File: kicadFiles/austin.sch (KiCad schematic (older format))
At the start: 465 parts, among them J1 TYPE-C-31-M12_13, J2 Conn_01x04_Male, J5 Conn_01x06_Male, Q1 AO4406AL, SW1 MXSwitch, SW10 MXSwitch, SW100 MXSwitch, SW101 MXSwitch, SW102 MXSwitch, SW103 MXSwitch, SW104 MXSwitch, SW105 MXSwitch, SW106 MXSwitch, SW107 MXSwitch, SW108 MXSwitch, SW109 MXSwitch, SW11 MXSwitch, SW110 MXSwitch, SW111 MXSwitch, SW112 MXSwitch, SW12 MXSwitch, SW13 MXSwitch, SW14 MXSwitch, SW15 MXSwitch, SW16 MXSwitch, SW17 MXSwitch, SW18 MXSwitch, SW19 MXSwitch, SW2 MXSwitch, SW20 MXSwitch, SW21 MXSwitch, SW22 MXSwitch, SW23 MXSwitch, SW24 MXSwitch, SW25 MXSwitch, SW26 MXSwitch, SW27 MXSwitch, SW28 MXSwitch, SW29 MXSwitch, SW3 MXSwitch, SW30 MXSwitch, SW31 MXSwitch, SW32 MXSwitch, SW33 MXSwitch, SW34 MXSwitch, SW35 MXSwitch, SW36 MXSwitch, SW37 MXSwitch, SW38 MXSwitch, SW39 MXSwitch, SW4 MXSwitch, SW40 MXSwitch, SW41 MXSwitch, SW42 MXSwitch, SW43 MXSwitch, SW44 MXSwitch, SW45 MXSwitch, SW46 MXSwitch, SW47 MXSwitch, SW48 MXSwitch, SW49 MXSwitch, SW5 MXSwitch, SW50 MXSwitch, SW51 MXSwitch, SW52 MXSwitch, SW53 MXSwitch, SW54 MXSwitch, SW55 MXSwitch, SW56 MXSwitch, SW57 MXSwitch, SW58 MXSwitch, SW59 MXSwitch, SW6 MXSwitch, SW60 MXSwitch, SW61 MXSwitch, SW62 MXSwitch, SW63 MXSwitch, SW64 MXSwitch, SW65 MXSwitch, SW66 MXSwitch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

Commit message: [Pre-release] V1.0 pre-release
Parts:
- added LEDCAPS1, LEDNUM1, LEDSCRL1: LED, acheronComponents:thtLED, symbol acheronSymbols:LED
- added RI1, RI2, RI3: 360, acheronComponents:R_1026, symbol Device:R_Small
- CB4: renamed from CVB4; value 1u -> 100n
- CB5: renamed from CVB5; value 4.7u -> 10u
- SW111: footprint acheronKeyboardSwitches:MX700 -> acheronKeyboardSwitches:MX700R
- renumbered CVB1 to CB1, CVB2 to CB2, CVB3 to CB3, CSin1 to CRI1, CSout1 to CRO1, D63 to D100, D65 to D101, D66 to D102, D71 to D103, D79 to D104, D85 to D105, D91 to D106, D97 to D107, D103 to D108, D67 to D13, D72 to D14, D75 to D15, D80 to D16, D86 to D17, D92 to D18, D98 to D19, D13 to D20, D14 to D21, D15 to D22, D16 to D23, D17 to D24, D18 to D25, D19 to D26, D20 to D27, D21 to D28, D22 to D29, D23 to D30, D24 to D31, D68 to D32, D73 to D33, D76 to D35, D81 to D36, D87 to D37, D93 to D38, D99 to D39, D25 to D40, D26 to D41, D27 to D42, D28 to D43, D29 to D44, D30 to D45, D31 to D46, D32 to D47, D33 to D48, D34 to D49, D35 to D50, D36 to D51, D69 to D52, D74 to D53, D77 to D54, D82 to D55, D88 to D56, D94 to D57, D100 to D59, D37 to D61, D38 to D62, D39 to D63, D40 to D64, D41 to D65, D42 to D66, D43 to D67, D44 to D68, D45 to D69, D46 to D70, D47 to D71, D104 to D72, D48 to D73, D78 to D74, D83 to D75, D89 to D76, D95 to D77, D101 to D78, D49 to D79, D51 to D80, D53 to D81, D55 to D82, D56 to D83, D57 to D84, D59 to D85, D60 to D86, D61 to D87, D62 to D88, D64 to D89, D105 to D90, D70 to D91, D84 to D92, D90 to D93, D96 to D94, D102 to D95, D50 to D96, D52 to D97, D54 to D98, D58 to D99, RPGate1 to RGP1, RSGate1 to RGS1, R72 to RL72
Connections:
- net labels added: CAPSLCK, NUMLCK, SCRLLCK
- wire segments 943 -> 952
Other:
- note added: "CBs for "Capacitors - Bypass""
- note added: "DF for "Diode - Fuse""
- note added: "DS33 for "Schottky Diode - 3.3V""
- note added: "RGP for "Gate Parallel"\nRGS for "Gate Series""

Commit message: [Update] Version 1.1
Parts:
- removed U2: MCP1700-3302E_SOT23, Package_TO_SOT_SMD:SOT-23, symbol Regulator_Linear:MCP1700-3302E_SOT23
- added U2: TLV1117-33, Package_TO_SOT_SMD:SOT-223-3_TabPin2, symbol Regulator_Linear:TLV1117-33
- U3: footprint Package_TO_SOT_SMD:SOT-23-6 -> acheronComponents:SOT-23-6
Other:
- note added: "CRI for Capacitor - Regulator Input"
- note added: "CRO for Capacitor - Regulator Output"
- moved on the sheet: CRI1, CRO1, DF1, DS33, F1
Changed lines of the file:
@@
 L Device:Polyfuse_Small F1
 U 1 1 5C25B88F
-P 15775 9850
-F 0 "F1" V 15614 9850 31  0000 C CNN
-F 1 "1A" V 15676 9850 31  0000 C CNN
-F 2 "Fuse:Fuse_1812_4532Metric_Pad1.30x3.40mm_HandSolder" H 15825 9650 50  0001 L CNN
-F 3 "~" H 15775 9850 50  0001 C CNN
-	1    15775 9850
+P 15775 9525
+F 0 "F1" V 15614 9525 31  0000 C CNN
+F 1 "1A" V 15676 9525 31  0000 C CNN
+F 2 "Fuse:Fuse_1812_4532Metric_Pad1.30x3.40mm_HandSolder" H 15825 9325 50  0001 L CNN
+F 3 "~" H 15775 9525 50  0001 C CNN
+	1    15775 9525
 	0    1    1    0
 $EndComp
-Text Notes 15650 9900 0    20   ~ 0
+Text Notes 15650 9575 0    20   ~ 0
 Polyfuse PPTC RTC
 $Comp
 L Device:D_Schottky_Small DF1
 U 1 1 5C2FFE6A
-P 16025 10000
-F 0 "DF1" V 16025 9825 31  0000 L CNN
-F 1 "RB060M-60TR" V 16100 9625 31  0000 L CNN
-F 2 "acheronComponents:D_SOD-123" V 16025 10000 50  0001 C CNN
-F 3 "~" V 16025 10000 50  0001 C CNN
-	1    16025 10000
+P 16025 9675
+F 0 "DF1" V 16025 9500 31  0000 L CNN
+F 1 "RB060M-60TR" V 16100 9300 31  0000 L CNN
+F 2 "acheronComponents:D_SOD-123" V 16025 9675 50  0001 C CNN
+F 3 "~" V 16025 9675 50  0001 C CNN
+	1    16025 9675
 	0    1    1    0
 $EndComp
 Wire Wire Line
-	15875 9850 16025 9850
+	15875 9525 16025 9525
 Wire Wire Line
-	16025 9850 16025 9900
-Connection ~ 16025 9850
+	16025 9525 16025 9575
+Connection ~ 16025 9525
 Wire Wire Line
-	16025 10100 16025 10150
+	16025 9775 16025 9825
 $Comp
 L power:GND #PWR016
 U 1 1 5C363806
-P 16025 10150
-F 0 "#PWR016" H 16025 9900 50  0001 C CNN
-F 1 "GND" V 16030 10022 50  0000 R CNN
-F 2 "" H 16025 10150 50  0001 C CNN
-F 3 "" H 16025 10150 50  0001 C CNN
-	1    16025 10150
+P 16025 9825
+F 0 "#PWR016" H 16025 9575 50  0001 C CNN
+F 1 "GND" V 16030 9697 50  0000 R CNN
+F 2 "" H 16025 9825 50  0001 C CNN
+F 3 "" H 16025 9825 50  0001 C CNN
+	1    16025 9825
 	1    0    0    -1
 $EndComp
@@
 L Device:C_Small CRI1
 U 1 1 5C44CEDC
-P 16250 10200
-F 0 "CRI1" V 16350 10200 39  0000 C CNN
-F 1 "100n" V 16150 10200 31  0000 C CNN
-F 2 "Capacitor_SMD:C_0805_2012Metric_Pad1.15x1.40mm_HandSolder" H 16250 10200 50  0001 C CNN
-F 3 "~" H 16250 10200 50  0001 C CNN
-	1    16250 10200
+P 16250 9875
+F 0 "CRI1" V 16350 9875 39  0000 C CNN
+F 1 "100n" V 16150 9875 31  0000 C CNN
+F 2 "Capacitor_SMD:C_0805_2012Metric_Pad1.15x1.40mm_HandSolder" H 16250 9875 50  0001 C CNN
+F 3 "~" H 16250 9875 50  0001 C CNN
+	1    16250 9875
 	-1   0    0    1
 $EndComp
@@
 L Device:D DS33
 U 1 1 5C44EA7A
-P 16600 9375
-F 0 "DS33" V 16569 9454 31  0000 L CNN
-F 1 "1N4007" V 16631 9454 31  0000 L CNN
-F 2 "Diode_SMD:D_SOD-123F" H 16600 9375 50  0001 C CNN
-F 3 "~" H 16600 9375 50  0001 C CNN
-	1    16600 9375
+P 16600 9050
+F 0 "DS33" V 16569 9129 31  0000 L CNN
+F 1 "1N4007" V 16631 9129 31  0000 L CNN
+F 2 "Diode_SMD:D_SOD-123F" H 16600 9050 50  0001 C CNN
+F 3 "~" H 16600 9050 50  0001 C CNN
+	1    16600 9050
 	1    0    0    -1
 $EndComp
@@
 L Device:C_Small CRO1
 U 1 1 5C44DAFA
-P 16950 10225
-F 0 "CRO1" V 17050 10225 39  0000 C CNN
-F 1 "100n" V 16825 10225 39  0000 C CNN
-F 2 "Capacitor_SMD:C_0805_2012Metric_Pad1.15x1.40mm_HandSolder" H 16950 10225 50  0001 C CNN
-F 3 "~" H 16950 10225 50  0001 C CNN
-	1    16950 10225
+P 16950 9900
+F 0 "CRO1" V 17050 9900 39  0000 C CNN
+F 1 "100n" V 16825 9900 39  0000 C CNN
+F 2 "Capacitor_SMD:C_0805_2012Metric_Pad1.15x1.40mm_HandSolder" H 16950 9900 50  0001 C CNN
+F 3 "~" H 16950 9900 50  0001 C CNN
+	1    16950 9900
 	-1   0    0    1
 $EndComp
 Wire Wire Line
-	16950 9850 16950 10125
+	16950 9525 16950 9800
 Wire Wire Line
-	16300 9850 16250 9850
+	16300 9525 16250 9525
 Wire Wire Line
-	16250 9850 16250 10100
-Connection ~ 16250 9850
+	16250 9525 16250 9775
+Connection ~ 16250 9525
 Wire Wire Line
-	16250 9850 16250 9375
+	16250 9525 16250 9050
 Wire Wire Line
-	16025 9850 16250 9850
+	16025 9525 16250 9525
 NoConn ~ 9225 11975
 NoConn ~ 9225 11875
@@
 Wire Wire Line
 	9300 10925 9300 10825
-Text GLabel 17250 9850 2    50   Output ~ 0
+Text GLabel 17250 9525 2    50   Output ~ 0
 3.3V
 Text GLabel 19375 12125 0    50   BiDi ~ 0
@@
 Wire Wire Line
 	19375 12025 19425 12025
-$Comp
-L Regulator_Linear:MCP1700-3302E_SOT23 U2
-U 1 1 5D83639E
-P 16600 9850
-F 0 "U2" H 16600 10048 31  0000 C CNN
-F 1 "MCP1700-3302E_SOT23" H 16600 9986 31  0000 C CNN
-F 2 "Package_TO_SOT_SMD:SOT-23" H 16600 10075 50  0001 C CNN
-F 3 "http://ww1.microchip.com/downloads/en/DeviceDoc/20001826C.pdf" H 16600 9850 50  0001 C CNN
-	1    16600 9850
-	1    0    0    -1
-$EndComp
 Wire Wire Line
-	16250 10300 16250 10450
+	16250 9975 16250 10125
 Wire Wire Line
-	16950 10450 16950 10325
+	16950 10125 16950 10000
 Wire Wire Line
-	16600 10150 16600 10450
-Connection ~ 16600 10450
+	16600 9825 16600 10125
+Connection ~ 16600 10125
 Wire Wire Line
-	16900 9850 16950 9850
+	16900 9525 16950 9525
 $Comp
 L power:GND #PWR018
 U 1 1 5D9C16B4
-P 16600 10525
-F 0 "#PWR018" H 16600 10275 50  0001 C CNN
-F 1 "GND" H 16605 10397 50  0000 R CNN
-F 2 "" H 16600 10525 50  0001 C CNN
-F 3 "" H 16600 10525 50  0001 C CNN
-	1    16600 10525
+P 16600 10200
+F 0 "#PWR018" H 16600 9950 50  0001 C CNN
+F 1 "GND" H 16605 10072 50  0000 R CNN
+F 2 "" H 16600 10200 50  0001 C CNN
+F 3 "" H 16600 10200 50  0001 C CNN
+	1    16600 10200
 	1    0    0    -1
 $EndComp
 Wire Wire Line
-	16600 10525 16600 10450
+	16600 10200 16600 10125
 Text GLabel 19975 10025 0    50   Input ~ 0
 3.3V
@@
 Text GLabel 9675 9675 2    50   Output ~ 0
 VBUS
-Text GLabel 15625 9850 0    50   Input ~ 0
+Text GLabel 15625 9525 0    50   Input ~ 0
 VBUS
 Wire Wire Line
-	15625 9850 15675 9850
+	15625 9525 15675 9525
 Text Notes 15200 10900 0    100  Italic 20
 Power supply and protection circuit
 Wire Wire Line
 	9225 9675 9325 9675
-Text GLabel 16025 9775 1    50   Output ~ 0
+Text GLabel 16025 9450 1    50   Output ~ 0
 5V
 Wire Wire Line
-	16025 9775 16025 9850
+	16025 9450 16025 9525
 Text GLabel 775  8900 1    50   Input ~ 0
 5V
@@
 Voltage regulation\ncapacitor bank\n
 Wire Wire Line
-	16750 9375 16950 9375
+	16750 9050 16950 9050
 Wire Wire Line
-	16250 9375 16450 9375
+	16250 9050 16450 9050
 Wire Wire Line
-	16950 9850 16950 9375
-Connection ~ 16950 9850
+	16950 9525 16950 9050
+Connection ~ 16950 9525
 Wire Wire Line
-	16600 10450 16950 10450
+	16600 10125 16950 10125
 Wire Wire Line
-	16950 9850 17250 9850
+	16950 9525 17250 9525
 Wire Wire Line
-	16600 10450 16250 10450
+	16600 10125 16250 10125
 Text Notes 8000 13175 0    50   ~ 0
 Shield\nnet
@@
 	7425 13975 9825 13975
 Wire Notes Line width 20
-	15150 9050 18000 9050
-Wire Notes Line width 20
 	15375 11275 15375 12550
 Wire Notes Line width 20
@@
 MCU
 Wire Notes Line width 20
-	18075 9075 18075 11025
-Wire Notes Line width 20
-	15100 9050 15100 11025
-Wire Notes Line width 20
 	15100 11025 18075 11025
 $Comp
@@
 F 0 "U3" V 10850 13450 50  0000 L CNN
 F 1 "USBLC6-2SC6" V 11000 13400 50  0000 L CNN
-F 2 "Package_TO_SOT_SMD:SOT-23-6" H 10450 13350 50  0001 C CNN
+F 2 "acheronComponents:SOT-23-6" H 10450 13350 50  0001 C CNN
 F 3 "http://www2.st.com/resource/en/datasheet/CD00050750.pdf" H 11400 13300 50  0001 C CNN
 	1    11200 12950
@@
 Text Notes 16550 12325 0    50   ~ 0
 CBs for "Capacitors - Bypass"
-Text Notes 15175 10675 0    50   ~ 0
+Text Notes 15150 10700 0    30   ~ 0
 DF for "Diode - Fuse"
-Text Notes 15175 10575 0    50   ~ 0
+Text Notes 15150 10625 0    30   ~ 0
 DS33 for "Schottky Diode - 3.3V"
 Wire Wire Line
@@
 Text GLabel 21650 12475 2    50   Input ~ 0
 NUMLCK
+$Comp
+L Regulator_Linear:TLV1117-33 U2
+U 1 1 5D21E92D
+P 16600 9525
+F 0 "U2" H 16600 9767 50  0000 C CNN
+F 1 "TLV1117-33" H 16600 9676 50  0000 C CNN
+F 2 "Package_TO_SOT_SMD:SOT-223-3_TabPin2" H 16600 9525 50  0001 C CNN
+F 3 "http://www.ti.com/lit/ds/symlink/tlv1117.pdf" H 16600 9525 50  0001 C CNN
+	1    16600 9525
+	1    0    0    -1
+$EndComp
+Text Notes 15150 10550 0    30   ~ 0
+CRI for Capacitor - Regulator Input
+Text Notes 15150 10475 0    30   ~ 0
+CRO for Capacitor - Regulator Output
+Wire Notes Line width 20
+	18075 8750 18075 11025
+Wire Notes Line width 20
+	15100 8750 15100 11025
+Wire Notes Line width 20
+	15100 8750 18075 8750
 $EndSCHEMATC

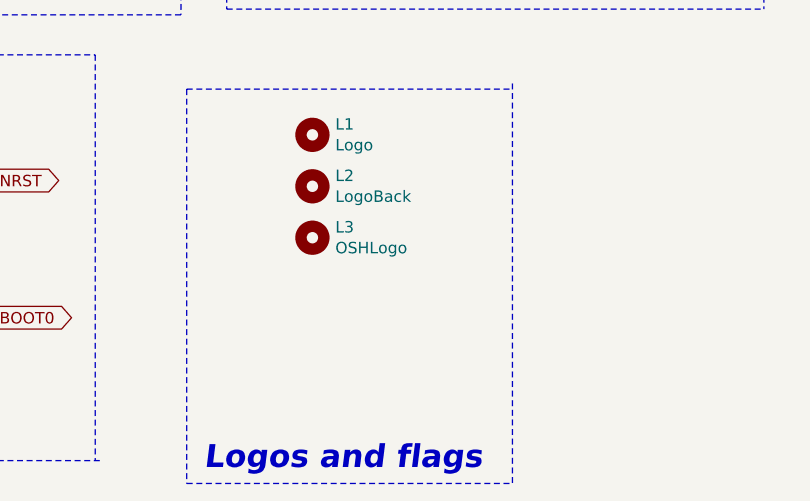
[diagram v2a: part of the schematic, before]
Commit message: [Update] V1.2: plated logo, new easter egg
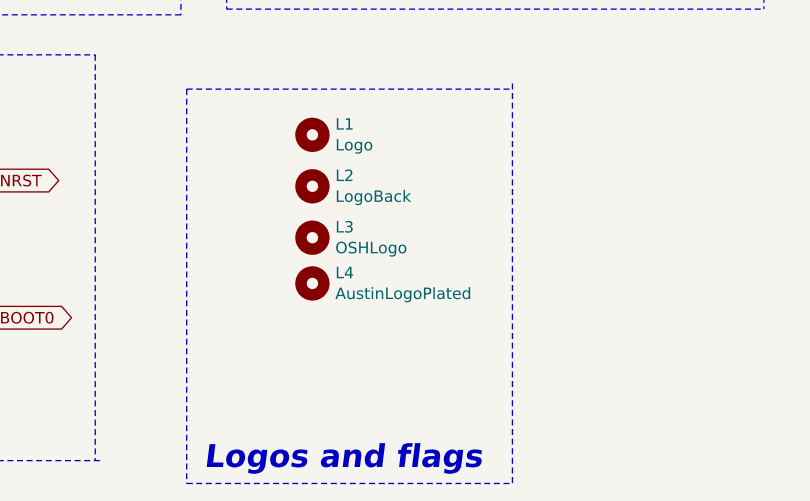
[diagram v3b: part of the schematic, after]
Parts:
- added L4: AustinLogoPlated, austinLogo:austinLogo_16x40_Plated, symbol Mechanical:MountingHole
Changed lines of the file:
@@
 Sheet 1 1
 Title "AustinPCB"
-Date "2019-06-06"
-Rev "1.0"
+Date "2019-06-20"
+Rev "1.2"
 Comp "Designed by Gondolindrim"
 Comment1 "In partnership with driftingbunnies and PheonixStar"
@@
 Wire Notes Line width 20
 	15100 8750 18075 8750
+$Comp
+L Mechanical:MountingHole L4
+U 1 1 5D1C668A
+P 10775 14975
+F 0 "L4" H 10875 15021 50  0000 L CNN
+F 1 "AustinLogoPlated" H 10875 14930 50  0000 L CNN
+F 2 "austinLogo:austinLogo_16x40_Plated" H 10775 14975 50  0001 C CNN
+F 3 "~" H 10775 14975 50  0001 C CNN
+	1    10775 14975
+	1    0    0    -1
+$EndComp
 $EndSCHEMATC

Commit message: Pre-release Alpha is publised
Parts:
- removed D78: 1N4148, acheronComponents:D_SOD-123, symbol Device:D
- removed L1: Logo, austinLogo:austinLogoSmall, symbol Mechanical:MountingHole
- removed LED59: LED, acheronComponents:thtLED, symbol acheronSymbols:LED
- removed SW58, SW78: MXSwitch, acheronKeyboardSwitches:MX100, symbol acheronSymbols:MXSwitch
- added L5: AustinLabel, austinLogo:austinLabel, symbol Mechanical:MountingHole
- added LED113: LED, acheronComponents:thtLED, symbol acheronSymbols:LED
- SW110: footprint acheronKeyboardSwitches:MX150 -> austinLogo:MX150
- SW111: footprint acheronKeyboardSwitches:MX700R -> austinLogo:MX700R
- SW59, SW95: footprint acheronKeyboardSwitches:MX200R -> austinLogo:MX200RV
- SW97: footprint acheronKeyboardSwitches:MX125 -> austinLogo:MX125
- SW99: footprint acheronKeyboardSwitches:MX625R -> austinLogo:MX625R
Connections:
- net GND: now also U1.10 (ADCIN2/PA0), U1.46 (SPI1_NSS/I2S2_WS/I2C1_SDA/PB9)
- net LEDK: now also LED113.K
- net Row3: no longer D59.1 (K)
- net Row4: now also D59.1 (K)
- net at LED109.A, RL96.2: now also LED113.A
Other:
- note removed: "Split+Down"
- note removed: "Split+Up"
- moved on the sheet: CB1, CB2, CB3, CB4, CB5, D59, SW59
